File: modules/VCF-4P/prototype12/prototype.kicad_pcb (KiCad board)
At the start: 6 copper layers, 40.6 x 78.7 mm, 30 parts, among them J1 Conn_01x09, U1 TL074, U2 SSI2140

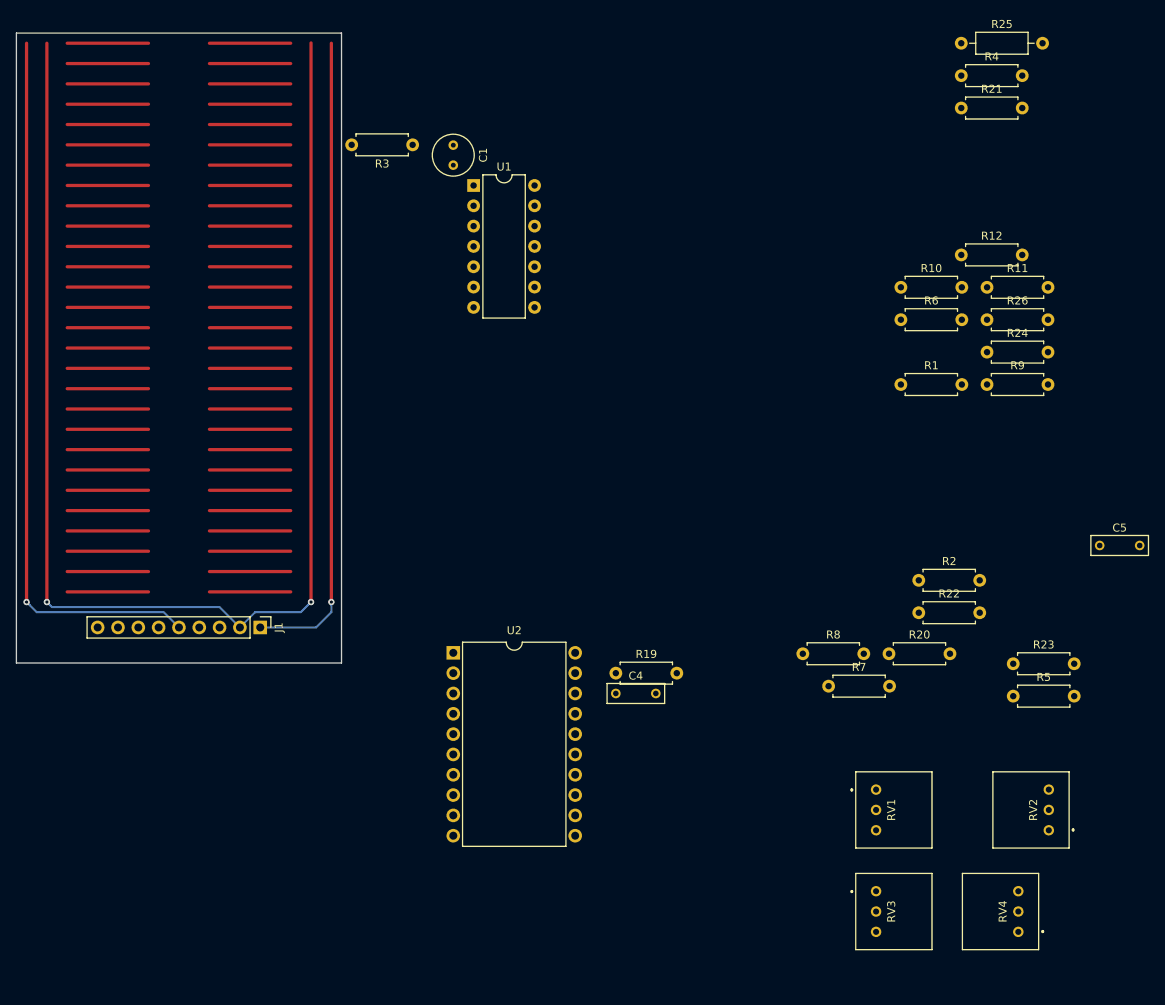
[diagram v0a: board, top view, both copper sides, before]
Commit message: VCF-4P: Breadboard prototype, 2-pole version - wip
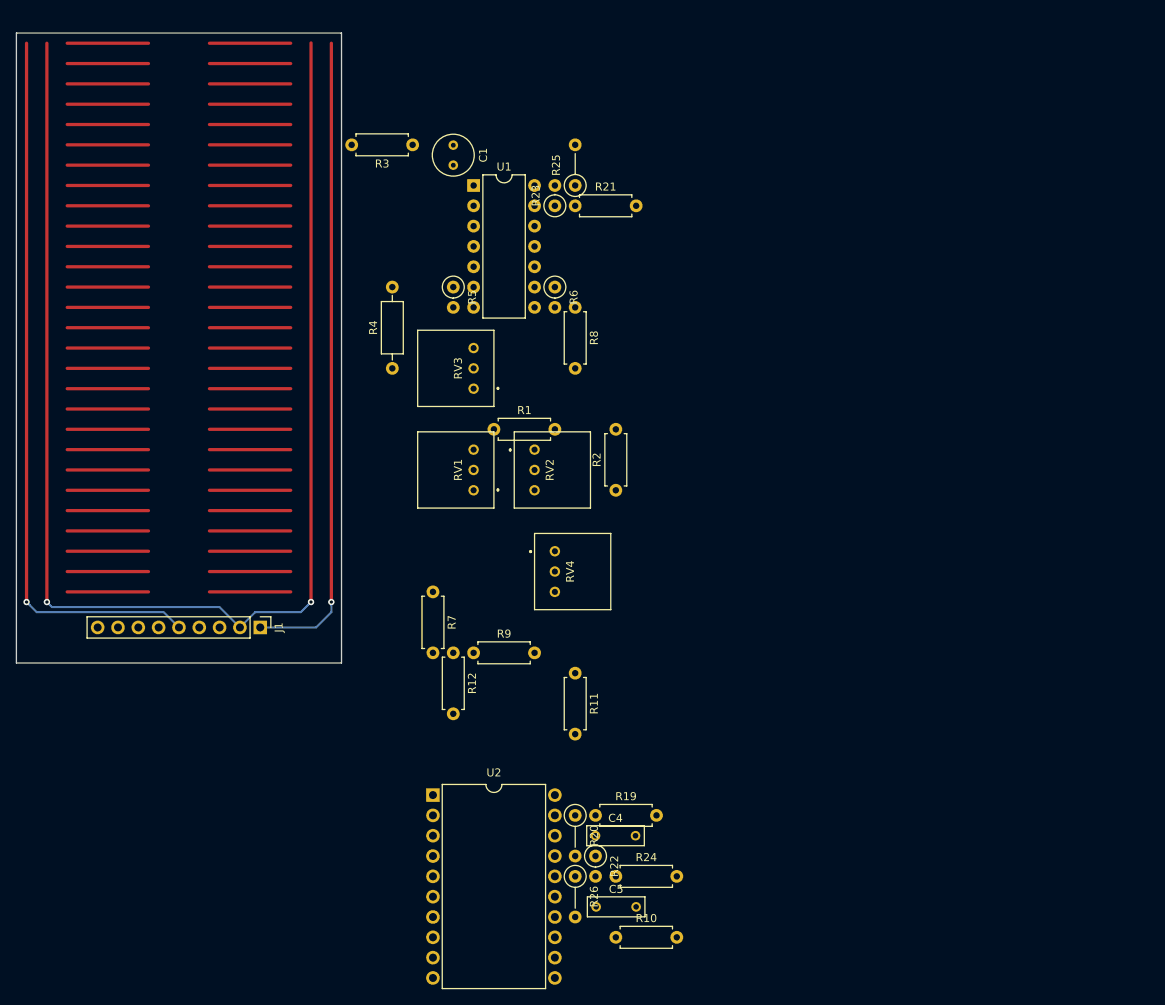
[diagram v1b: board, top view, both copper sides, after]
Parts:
- R20, R26: footprint -lmp-misc:R_Axial_DIN0207_L6.3mm_D2.5mm_P7.62mm_Horizontal -> -lmp-stripboard:SB_Gen_2
- R22, R23, R5, R6: footprint -lmp-misc:R_Axial_DIN0207_L6.3mm_D2.5mm_P7.62mm_Horizontal -> -lmp-stripboard:SB_Gen_1
- R25: footprint -lmp-misc:R_Axial_DIN0207_L6.3mm_D2.5mm_P10.16mm_Horizontal -> -lmp-stripboard:SB_Gen_2
- R4: footprint -lmp-misc:R_Axial_DIN0207_L6.3mm_D2.5mm_P7.62mm_Horizontal -> -lmp-stripboard:SB_Gen_4
- moved R10 88.7 mm to (157.5, 137.2)
- moved RV3 86.9 mm to (137.8, 66.0), turned to -90 degrees
- moved R5 86.7 mm to (137.2, 55.9), turned to -90 degrees
- moved R26 86.6 mm to (152.4, 129.5), turned to -90 degrees
- moved R23 81.0 mm to (149.9, 45.7), turned to 90 degrees
- moved R12 80.7 mm to (137.2, 101.6), turned to -90 degrees
- moved R24 80.3 mm to (157.5, 129.5)
- moved R4 80.0 mm to (129.5, 66.0), turned to 90 degrees
- moved C5 77.5 mm to (155.0, 133.3)
- moved RV2 73.9 mm to (149.2, 78.7), turned to 90 degrees
- moved R9 72.4 mm to (139.7, 101.6)
- moved R11 70.5 mm to (152.4, 104.1), turned to -90 degrees
- moved RV1 68.8 mm to (137.8, 78.7), turned to -90 degrees
- moved RV4 68.8 mm to (151.8, 91.4), turned to 90 degrees
- moved R8 51.8 mm to (152.4, 58.4), turned to -90 degrees
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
